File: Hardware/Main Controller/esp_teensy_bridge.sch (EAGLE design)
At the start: 47 parts, among them IC1 BQ79600PWRQ1, Q1 SI7611DN-T1-GE3, Q2 SI7611DN-T1-GE3, Q3 SI7611DN-T1-GE3, Q4 SI7611DN-T1-GE3

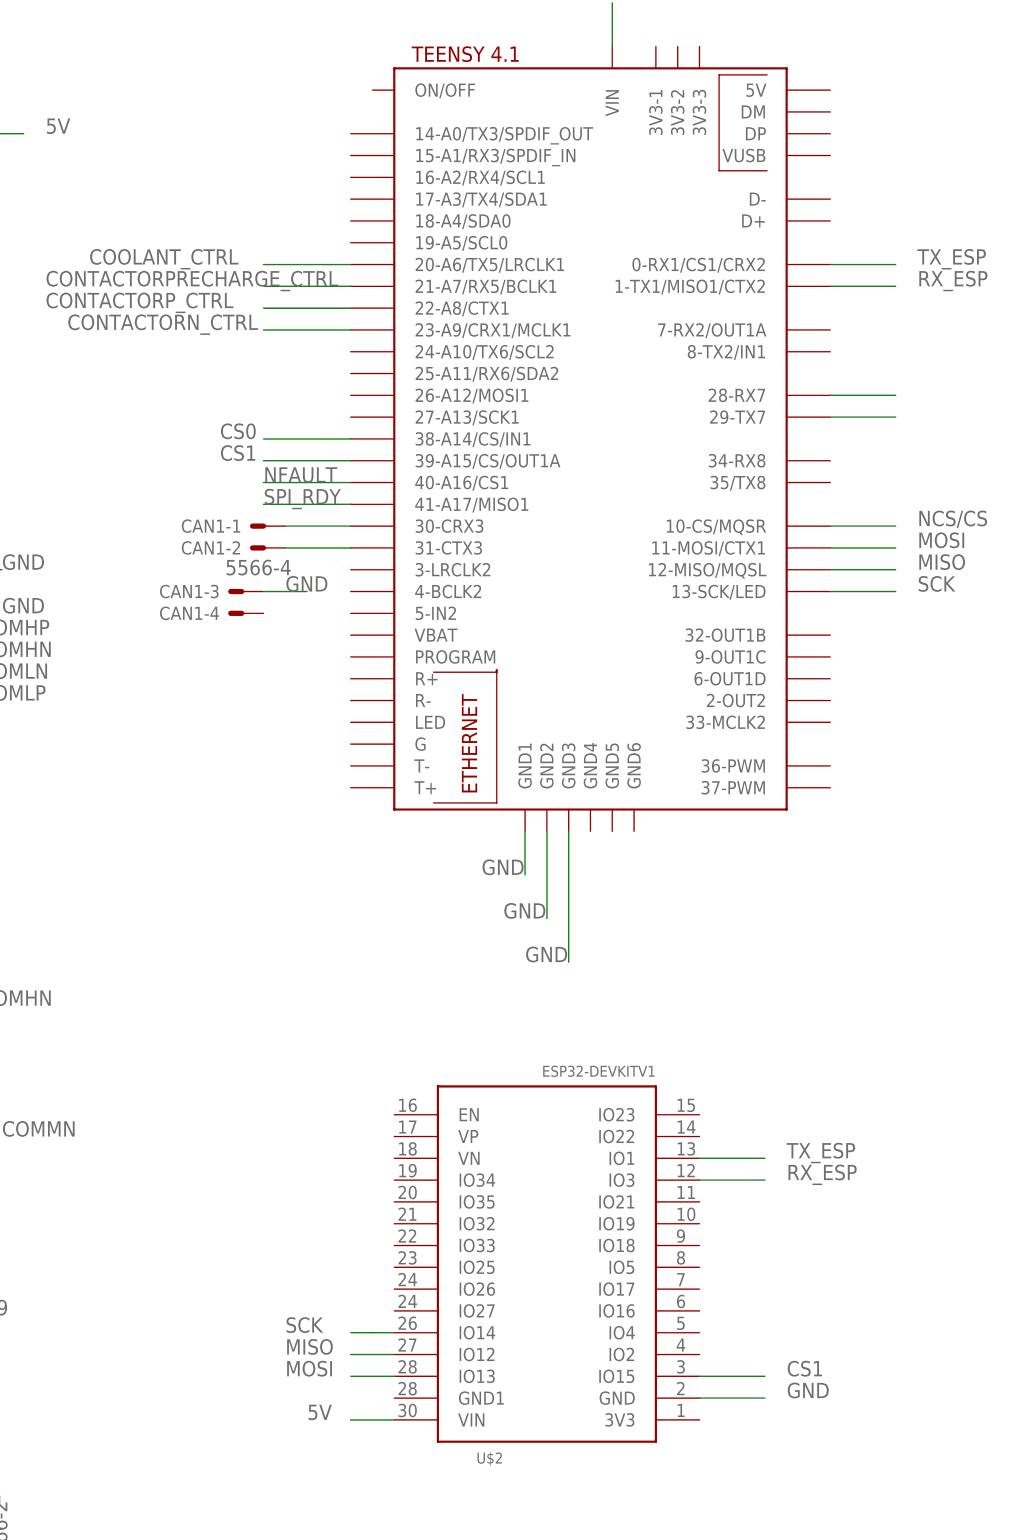
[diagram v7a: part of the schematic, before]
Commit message: seperate spi
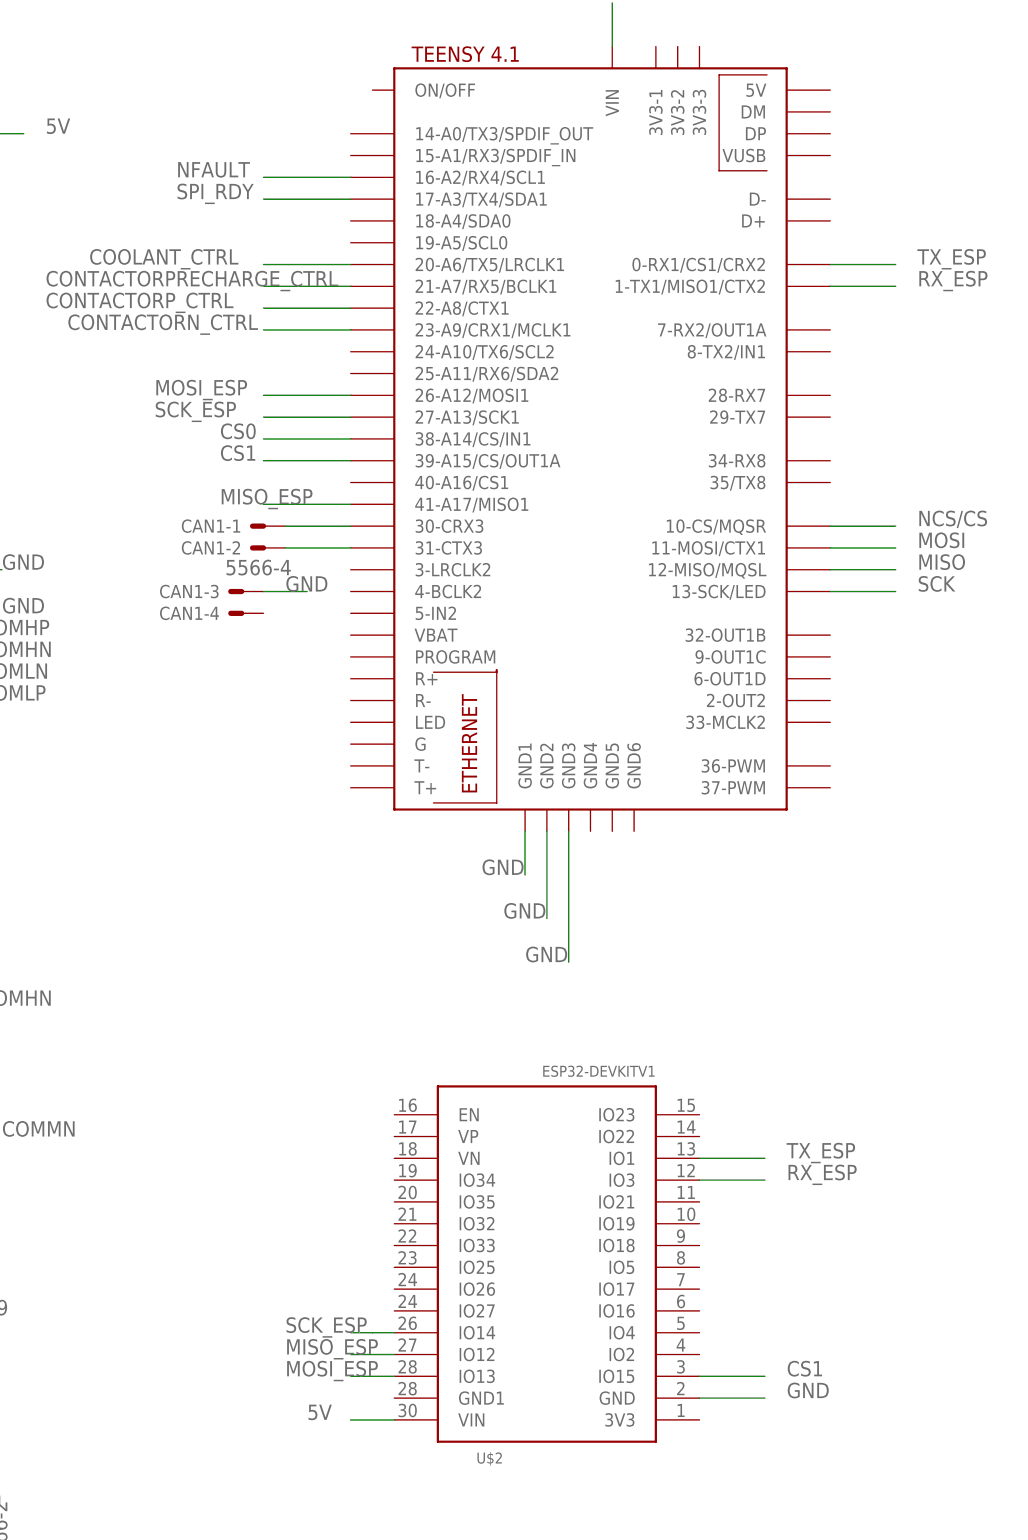
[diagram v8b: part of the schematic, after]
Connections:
- removed net RX_BRIDGE: U$3.29-TX7
- removed net TX_BRIDGE: U$3.28-RX7
- new net MISO_ESP: U$2.IO12, U$3.41-A17/MISO1
- new net MOSI_ESP: U$2.IO13, U$3.26-A12/MOSI1
- new net SCK_ESP: U$2.IO14, U$3.27-A13/SCK1
- net MISO: no longer U$2.IO12
- net MOSI: no longer U$2.IO13
- net NFAULT: now also U$3.16-A2/RX4/SCL1; no longer U$3.40-A16/CS1
- net SCK: no longer U$2.IO14
- net SPI_RDY: now also U$3.17-A3/TX4/SDA1; no longer U$3.41-A17/MISO1
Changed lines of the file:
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@@
-</segment>
-</net>
-<net name="TX_BRIDGE" class="0">
-<segment>
-<pinref part="U$3" gate="G$1" pin="28-RX7"/>
-<wire x1="96.52" y1="86.36" x2="104.14" y2="86.36" width="0.1524" layer="91"/>
-</segment>
-</net>
-<net name="RX_BRIDGE" class="0">
-<segment>
-<pinref part="U$3" gate="G$1" pin="29-TX7"/>
-<wire x1="96.52" y1="83.82" x2="104.14" y2="83.82" width="0.1524" layer="91"/>
 </segment>
 </net>
@@
 <label x="106.68" y="68.58" size="1.778" layer="95"/>
 </segment>
-<segment>
-<pinref part="U$2" gate="G$1" pin="IO13"/>
-<wire x1="45.72" y1="-27.94" x2="40.64" y2="-27.94" width="0.1524" layer="91"/>
-<label x="33.02" y="-27.94" size="1.778" layer="95"/>
-</segment>
 </net>
 <net name="MISO" class="0">
@@
 <label x="106.68" y="66.04" size="1.778" layer="95"/>
 </segment>
+</net>
+<net name="SCK" class="0">
+<segment>
+<pinref part="IC1" gate="G$1" pin="SCLK"/>
+<wire x1="-63.5" y1="53.34" x2="-76.2" y2="53.34" width="0.1524" layer="91"/>
+<label x="-81.28" y="53.34" size="1.778" layer="95"/>
+</segment>
+<segment>
+<pinref part="U$3" gate="G$1" pin="13-SCK/LED"/>
+<wire x1="96.52" y1="63.5" x2="104.14" y2="63.5" width="0.1524" layer="91"/>
+<label x="106.68" y="63.5" size="1.778" layer="95"/>
+</segment>
+</net>
+<net name="CS1" class="0">
+<segment>
+<pinref part="U$3" gate="G$1" pin="39-A15/CS/OUT1A"/>
+<wire x1="40.64" y1="78.74" x2="30.48" y2="78.74" width="0.1524" layer="91"/>
+<label x="25.4" y="78.74" size="1.778" layer="95"/>
+</segment>
+<segment>
+<pinref part="U$2" gate="G$1" pin="IO15"/>
+<wire x1="81.28" y1="-27.94" x2="88.9" y2="-27.94" width="0.1524" layer="91"/>
+<label x="91.44" y="-27.94" size="1.778" layer="95"/>
+</segment>
+</net>
+<net name="CS0" class="0">
+<segment>
+<pinref part="U$3" gate="G$1" pin="38-A14/CS/IN1"/>
+<wire x1="40.64" y1="81.28" x2="30.48" y2="81.28" width="0.1524" layer="91"/>
+<label x="25.4" y="81.28" size="1.778" layer="95"/>
+</segment>
+<segment>
+<pinref part="IC1" gate="G$1" pin="NCS"/>
+<wire x1="-63.5" y1="50.8" x2="-76.2" y2="50.8" width="0.1524" layer="91"/>
+<label x="-81.28" y="50.8" size="1.778" layer="95"/>
+<pinref part="R4" gate="G$1" pin="2"/>
+</segment>
+</net>
+<net name="NFAULT" class="0">
+<segment>
+<pinref part="IC1" gate="G$1" pin="NFAULT"/>
+<pinref part="R2" gate="G$1" pin="2"/>
+<wire x1="-63.5" y1="63.5" x2="-71.12" y2="63.5" width="0.1524" layer="91"/>
+<label x="-68.58" y="63.5" size="1.778" layer="95"/>
+</segment>
+<segment>
+<pinref part="U$3" gate="G$1" pin="16-A2/RX4/SCL1"/>
+<wire x1="40.64" y1="111.76" x2="30.48" y2="111.76" width="0.1524" layer="91"/>
+<label x="20.32" y="111.76" size="1.778" layer="95"/>
+</segment>
+</net>
+<net name="SPI_RDY" class="0">
+<segment>
+<pinref part="IC1" gate="G$1" pin="NUART/SPI_(SPI_RDY)"/>
+<pinref part="R3" gate="G$1" pin="2"/>
+<wire x1="-63.5" y1="48.26" x2="-68.58" y2="48.26" width="0.1524" layer="91"/>
+<label x="-68.58" y="48.26" size="1.778" layer="95"/>
+</segment>
+<segment>
+<pinref part="U$3" gate="G$1" pin="17-A3/TX4/SDA1"/>
+<wire x1="40.64" y1="109.22" x2="30.48" y2="109.22" width="0.1524" layer="91"/>
+<label x="20.32" y="109.22" size="1.778" layer="95"/>
+</segment>
+</net>
+<net name="MOSI_ESP" class="0">
+<segment>
+<pinref part="U$3" gate="G$1" pin="26-A12/MOSI1"/>
+<wire x1="40.64" y1="86.36" x2="30.48" y2="86.36" width="0.1524" layer="91"/>
+<label x="17.78" y="86.36" size="1.778" layer="95"/>
+</segment>
+<segment>
+<pinref part="U$2" gate="G$1" pin="IO13"/>
+<wire x1="45.72" y1="-27.94" x2="40.64" y2="-27.94" width="0.1524" layer="91"/>
+<label x="33.02" y="-27.94" size="1.778" layer="95"/>
+</segment>
+</net>
+<net name="MISO_ESP" class="0">
+<segment>
+<pinref part="U$3" gate="G$1" pin="41-A17/MISO1"/>
+<wire x1="40.64" y1="73.66" x2="30.48" y2="73.66" width="0.1524" layer="91"/>
+<label x="25.4" y="73.66" size="1.778" layer="95"/>
+</segment>
 <segment>
 <pinref part="U$2" gate="G$1" pin="IO12"/>
@@
 </segment>
 </net>
-<net name="SCK" class="0">
-<segment>
-<pinref part="IC1" gate="G$1" pin="SCLK"/>
-<wire x1="-63.5" y1="53.34" x2="-76.2" y2="53.34" width="0.1524" layer="91"/>
-<label x="-81.28" y="53.34" size="1.778" layer="95"/>
-</segment>
-<segment>
-<pinref part="U$3" gate="G$1" pin="13-SCK/LED"/>
-<wire x1="96.52" y1="63.5" x2="104.14" y2="63.5" width="0.1524" layer="91"/>
-<label x="106.68" y="63.5" size="1.778" layer="95"/>
+<net name="SCK_ESP" class="0">
+<segment>
+<pinref part="U$3" gate="G$1" pin="27-A13/SCK1"/>
+<wire x1="40.64" y1="83.82" x2="30.48" y2="83.82" width="0.1524" layer="91"/>
+<label x="17.78" y="83.82" size="1.778" layer="95"/>
 </segment>
 <segment>
@@
 </segment>
 </net>
-<net name="CS1" class="0">
-<segment>
-<pinref part="U$3" gate="G$1" pin="39-A15/CS/OUT1A"/>
-<wire x1="40.64" y1="78.74" x2="30.48" y2="78.74" width="0.1524" layer="91"/>
-<label x="25.4" y="78.74" size="1.778" layer="95"/>
-</segment>
-<segment>
-<pinref part="U$2" gate="G$1" pin="IO15"/>
-<wire x1="81.28" y1="-27.94" x2="88.9" y2="-27.94" width="0.1524" layer="91"/>
-<label x="91.44" y="-27.94" size="1.778" layer="95"/>
-</segment>
-</net>
-<net name="CS0" class="0">
-<segment>
-<pinref part="U$3" gate="G$1" pin="38-A14/CS/IN1"/>
-<wire x1="40.64" y1="81.28" x2="30.48" y2="81.28" width="0.1524" layer="91"/>
-<label x="25.4" y="81.28" size="1.778" layer="95"/>
-</segment>
-<segment>
-<pinref part="IC1" gate="G$1" pin="NCS"/>
-<wire x1="-63.5" y1="50.8" x2="-76.2" y2="50.8" width="0.1524" layer="91"/>
-<label x="-81.28" y="50.8" size="1.778" layer="95"/>
-<pinref part="R4" gate="G$1" pin="2"/>
-</segment>
-</net>
-<net name="NFAULT" class="0">
-<segment>
-<pinref part="IC1" gate="G$1" pin="NFAULT"/>
-<pinref part="R2" gate="G$1" pin="2"/>
-<wire x1="-63.5" y1="63.5" x2="-71.12" y2="63.5" width="0.1524" layer="91"/>
-<label x="-68.58" y="63.5" size="1.778" layer="95"/>
-</segment>
-<segment>
-<pinref part="U$3" gate="G$1" pin="40-A16/CS1"/>
-<wire x1="40.64" y1="76.2" x2="30.48" y2="76.2" width="0.1524" layer="91"/>
-<label x="30.48" y="76.2" size="1.778" layer="95"/>
-</segment>
-</net>
-<net name="SPI_RDY" class="0">
-<segment>
-<pinref part="IC1" gate="G$1" pin="NUART/SPI_(SPI_RDY)"/>
-<pinref part="R3" gate="G$1" pin="2"/>
-<wire x1="-63.5" y1="48.26" x2="-68.58" y2="48.26" width="0.1524" layer="91"/>
-<label x="-68.58" y="48.26" size="1.778" layer="95"/>
-</segment>
-<segment>
-<pinref part="U$3" gate="G$1" pin="41-A17/MISO1"/>
-<wire x1="40.64" y1="73.66" x2="30.48" y2="73.66" width="0.1524" layer="91"/>
-<label x="30.48" y="73.66" size="1.778" layer="95"/>
-</segment>
-</net>
